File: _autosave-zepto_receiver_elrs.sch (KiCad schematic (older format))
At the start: 43 parts, among them J1 u.fl, SW1 SW_Push, U1 STM32WLE5JBI6, U2 NCP160, U3 BGS12PL6E6327XTSA1, U4 0900FM15D0039, U5 ECS-TXO-25CSMV-320-AM-TR

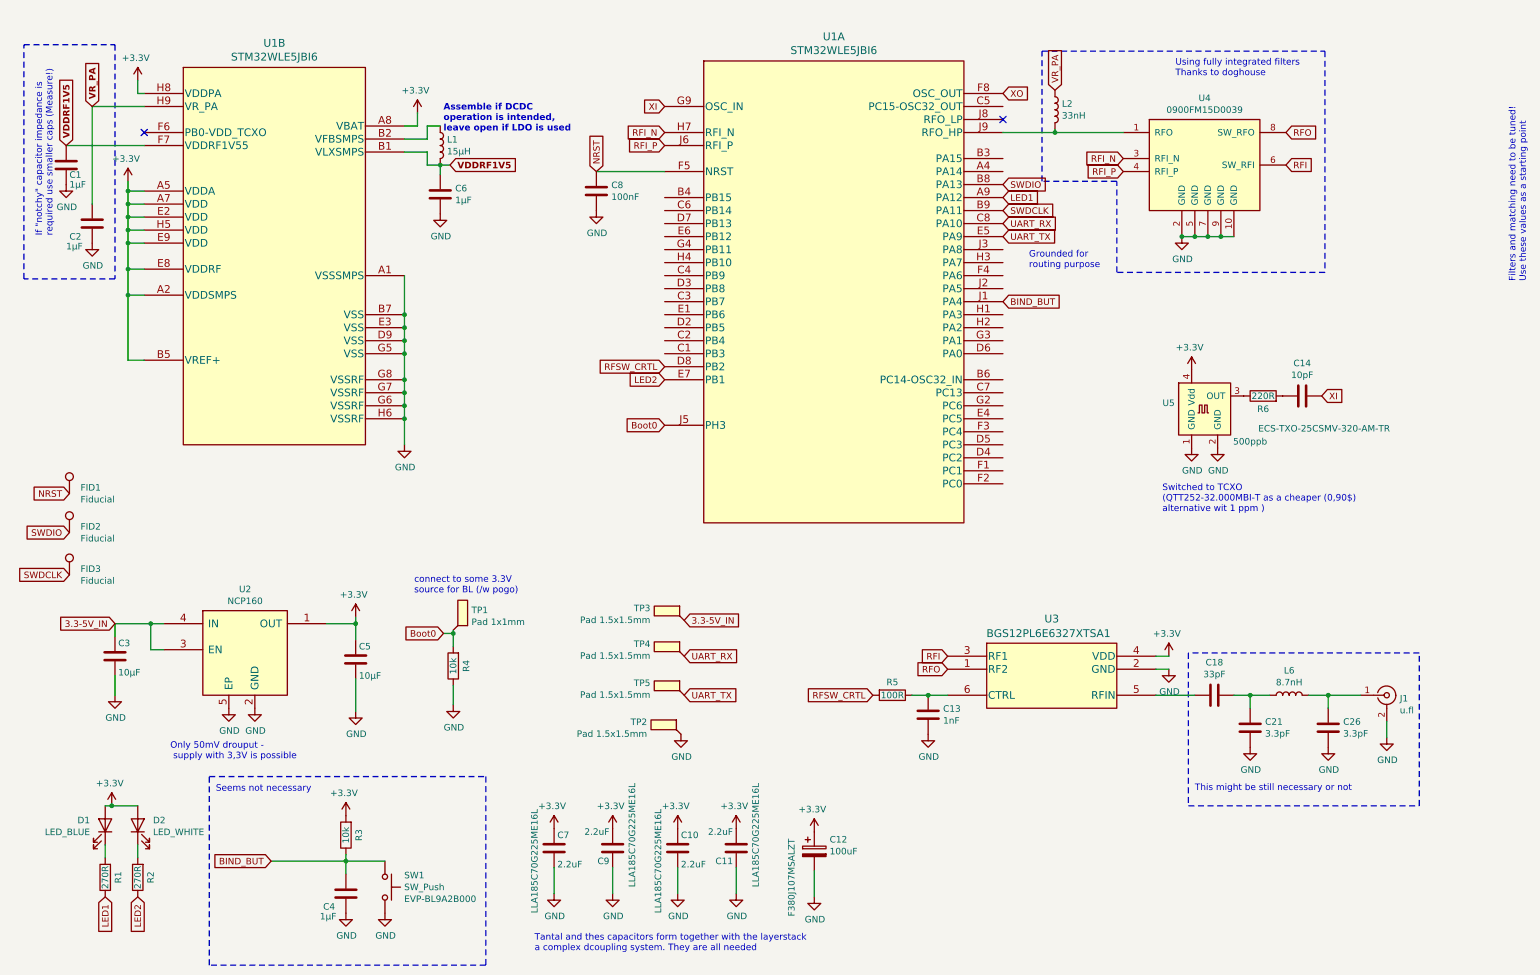
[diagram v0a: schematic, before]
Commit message: Shrinked down reciever to 9.5x7.5mm
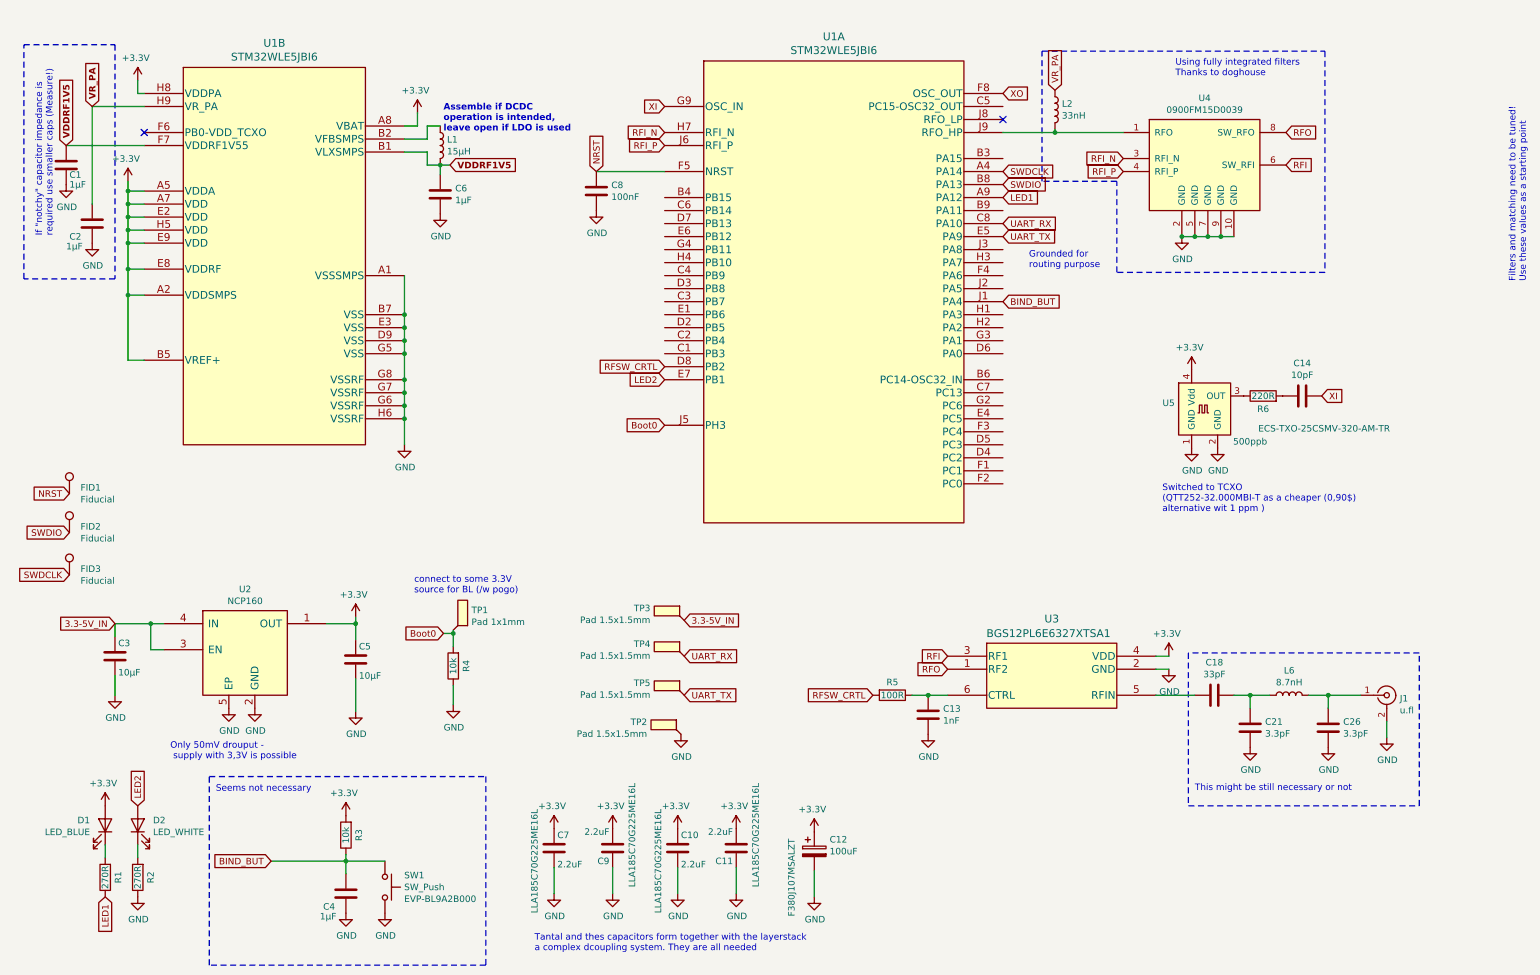
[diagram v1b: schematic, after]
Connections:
- net +3V3: no longer D2.2 (A)
- net GND: now also R2.1
- net LED2: now also D2.2 (A); no longer R2.1
- net SWDCLK: now also U1.A4 (PA14); no longer U1.B9 (PA11)
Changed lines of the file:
@@
 Comment4 ""
 $EndDescr
-$Comp
-L power:+3.3V #PWR03
-U 1 1 6081FD31
-P 1150 6525
-F 0 "#PWR03" H 1150 6375 50  0001 C CNN
-F 1 "+3.3V" H 1165 6698 50  0000 C CNN
-F 2 "" H 1150 6525 50  0001 C CNN
-F 3 "" H 1150 6525 50  0001 C CNN
-	1    1150 6525
-	-1   0    0    -1
-$EndComp
 Wire Wire Line
 	1100 6825 1100 6925
@@
 Text GLabel 1100 7225 3    50   Input ~ 0
 LED1
-Text GLabel 1350 7225 3    50   Input ~ 0
+Text GLabel 1350 6525 1    50   Input ~ 0
 LED2
-Wire Wire Line
-	1100 6525 1150 6525
-Connection ~ 1150 6525
-Wire Wire Line
-	1150 6525 1350 6525
 Text GLabel 8000 1850 2    50   Input ~ 0
 LED1
@@
 Text GLabel 8000 1750 2    50   Input ~ 0
 SWDIO
-Text GLabel 8000 1950 2    50   Input ~ 0
+Text GLabel 8000 1650 2    50   Input ~ 0
 SWDCLK
+$Comp
+L power:+3.3V #PWR03
+U 1 1 6081FD31
+P 1100 6525
+F 0 "#PWR03" H 1100 6375 50  0001 C CNN
+F 1 "+3.3V" H 1115 6698 50  0000 C CNN
+F 2 "" H 1100 6525 50  0001 C CNN
+F 3 "" H 1100 6525 50  0001 C CNN
+	1    1100 6525
+	-1   0    0    -1
+$EndComp
+$Comp
+L power:GND #PWR0101
+U 1 1 6058EF5F
+P 1350 7225
+F 0 "#PWR0101" H 1350 6975 50  0001 C CNN
+F 1 "GND" H 1355 7052 50  0000 C CNN
+F 2 "" H 1350 7225 50  0001 C CNN
+F 3 "" H 1350 7225 50  0001 C CNN
+	1    1350 7225
+	1    0    0    -1
+$EndComp
 $EndSCHEMATC
